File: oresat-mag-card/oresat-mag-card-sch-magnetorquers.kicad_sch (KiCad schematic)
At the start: 67 parts, among them U12 STSPIN250, U13 STSPIN250, U14 INA185, U15 INA185, U16 STSPIN250, U17 INA185

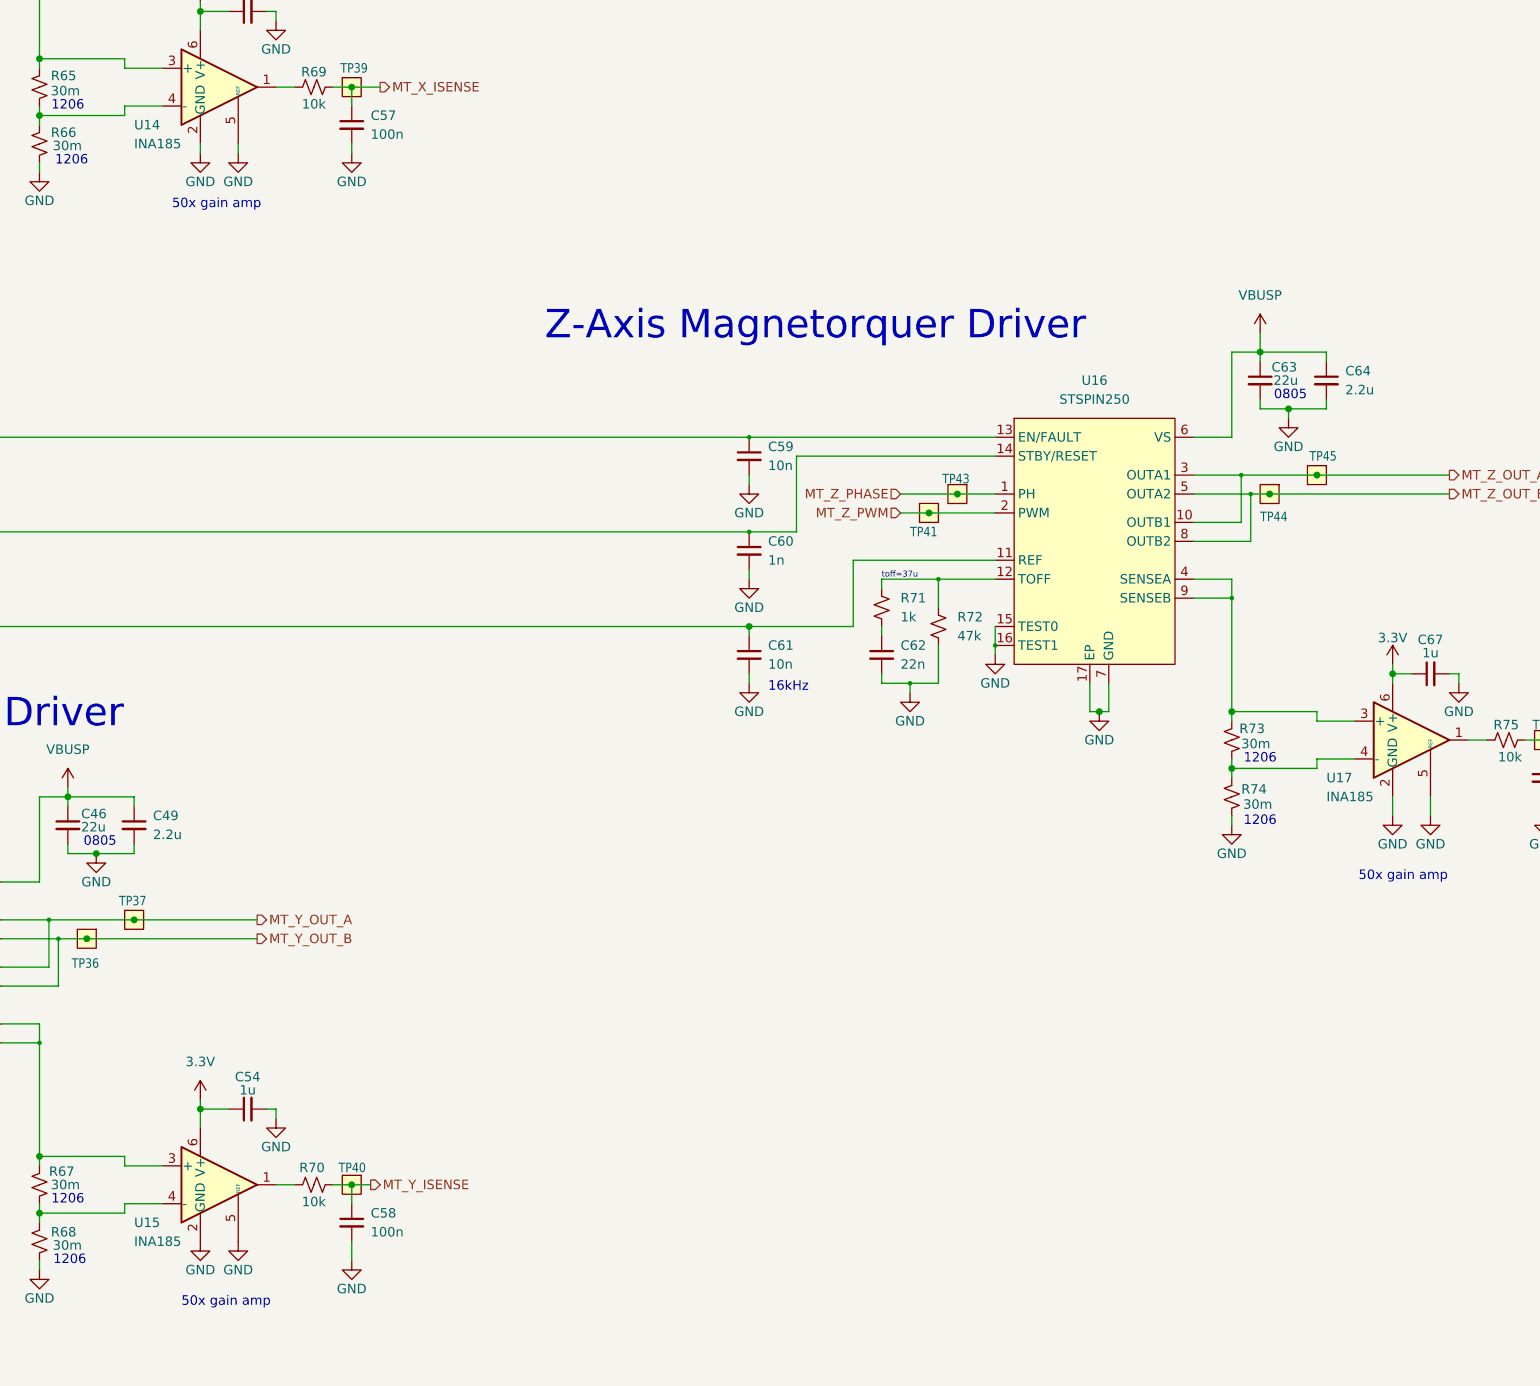
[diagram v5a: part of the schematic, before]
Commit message: Notes on current shunt gain
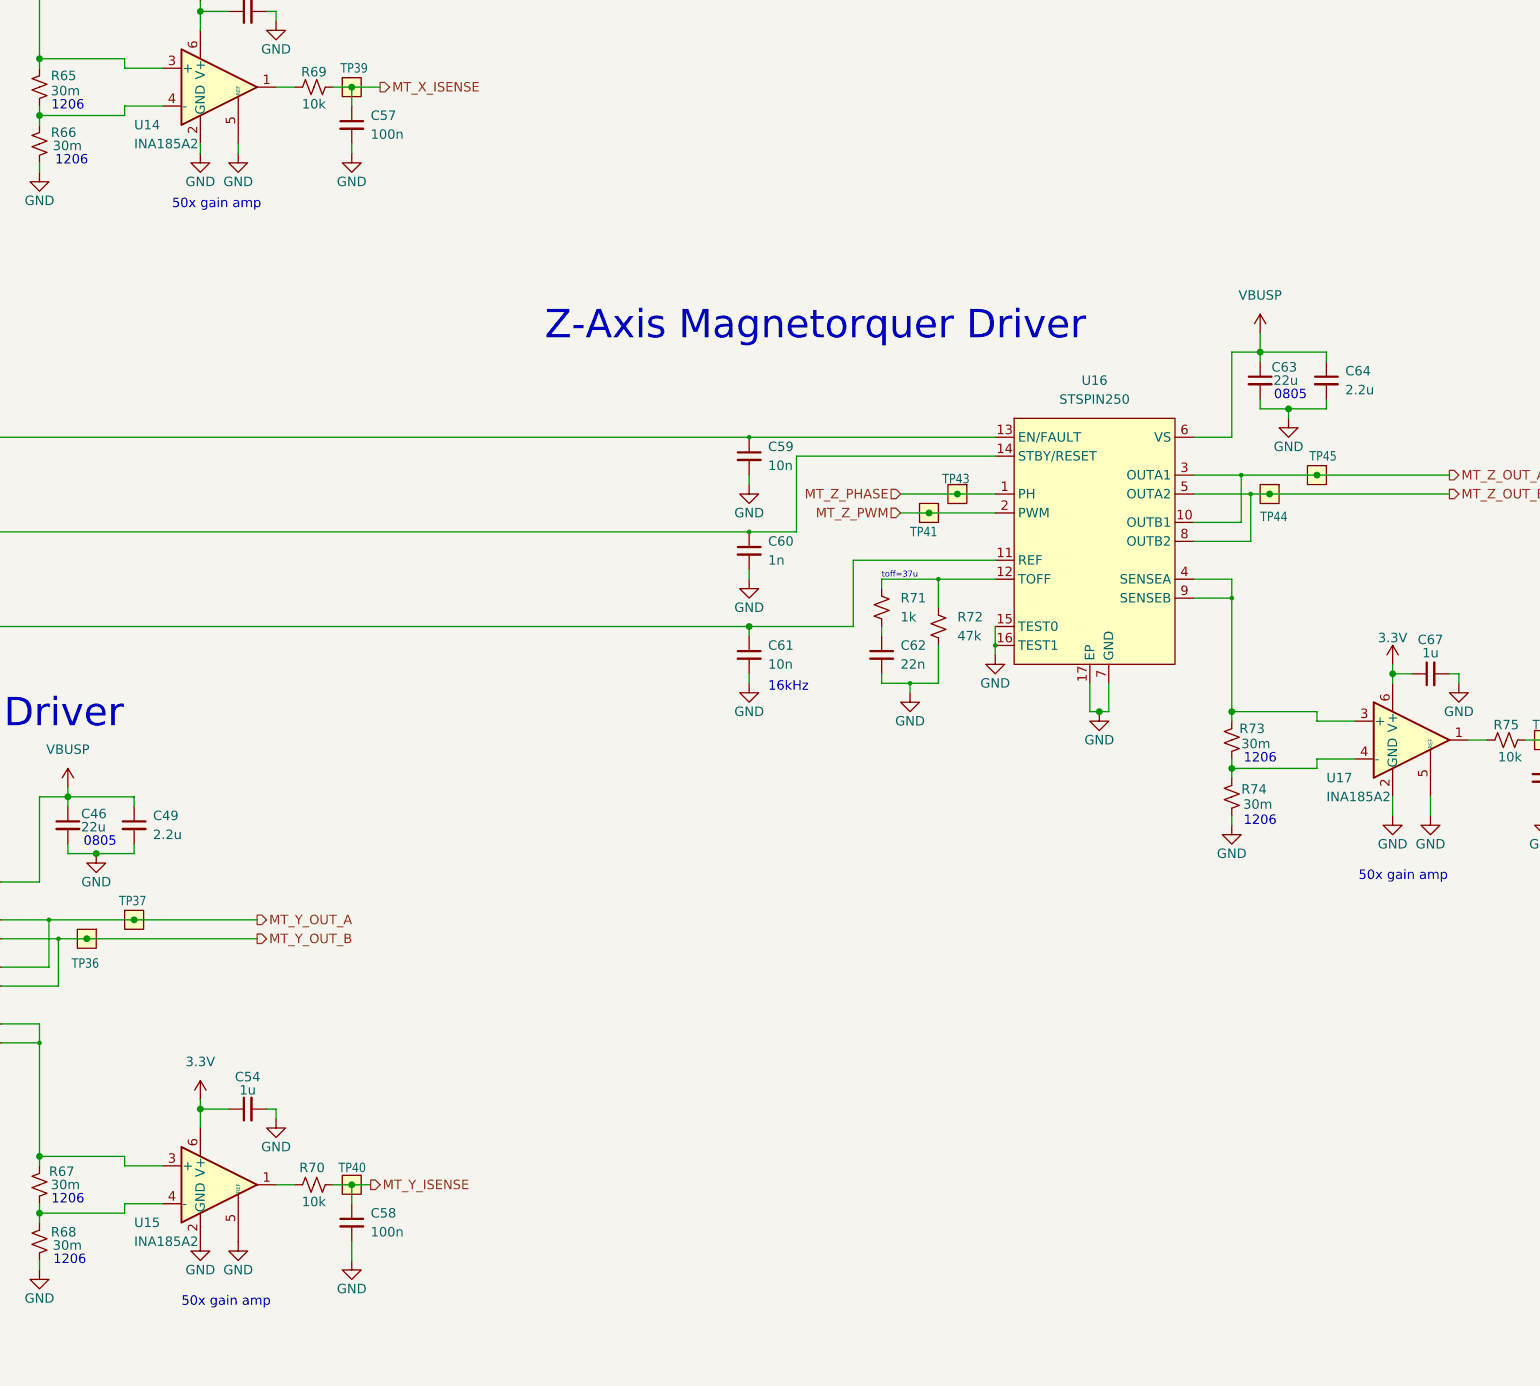
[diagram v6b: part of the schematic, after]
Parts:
- U14, U15, U17: value INA185 -> INA185A2
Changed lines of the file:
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@@
 			)
 		)
-		(property "Value" "INA185"
+		(property "Value" "INA185A2"
 			(at 191.77 91.4399 0)
 			(show_name no)
@@
 			)
 		)
-		(property "Value" "INA185"
+		(property "Value" "INA185A2"
 			(at 351.79 179.0699 0)
 			(show_name no)
@@
 			)
 		)
-		(property "Value" "INA185"
+		(property "Value" "INA185A2"
 			(at 191.77 238.7599 0)
 			(show_name no)
